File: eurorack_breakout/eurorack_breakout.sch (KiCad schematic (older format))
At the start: 11 parts, among them J1 Conn_02x08_Odd_Even, J2 Conn_01x08_Male, U1 LM1117-3.3, U2 LM1117-5.0

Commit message: eh, different license
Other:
- note added: "(c) 2021 Zachary Hart\nCC BY-SA-4.0\nrev0.1"
- note removed: "(c) 2021 Zachary Hart\nCC BY-NC-SA\n"
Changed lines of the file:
@@
 Text Notes 8400 7750 2    69   Italic 14
 16-Pin Eurorack Power Breakout
-Text Notes 6300 6950 0    49   ~ 0
-(c) 2021 Zachary Hart\nCC BY-NC-SA\n
+Text Notes 6300 7050 0    49   ~ 0
+(c) 2021 Zachary Hart\nCC BY-SA-4.0\nrev0.1
 $EndSCHEMATC

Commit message: board rev0.2
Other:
- note added: "(c) 2021 Zachary Hart\nCC BY-SA-4.0\nschematic rev0.1"
- note removed: "(c) 2021 Zachary Hart\nCC BY-SA-4.0\nrev0.1"
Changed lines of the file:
@@
 16-Pin Eurorack Power Breakout
 Text Notes 6300 7050 0    49   ~ 0
-(c) 2021 Zachary Hart\nCC BY-SA-4.0\nrev0.1
+(c) 2021 Zachary Hart\nCC BY-SA-4.0\nschematic rev0.1
 $EndSCHEMATC

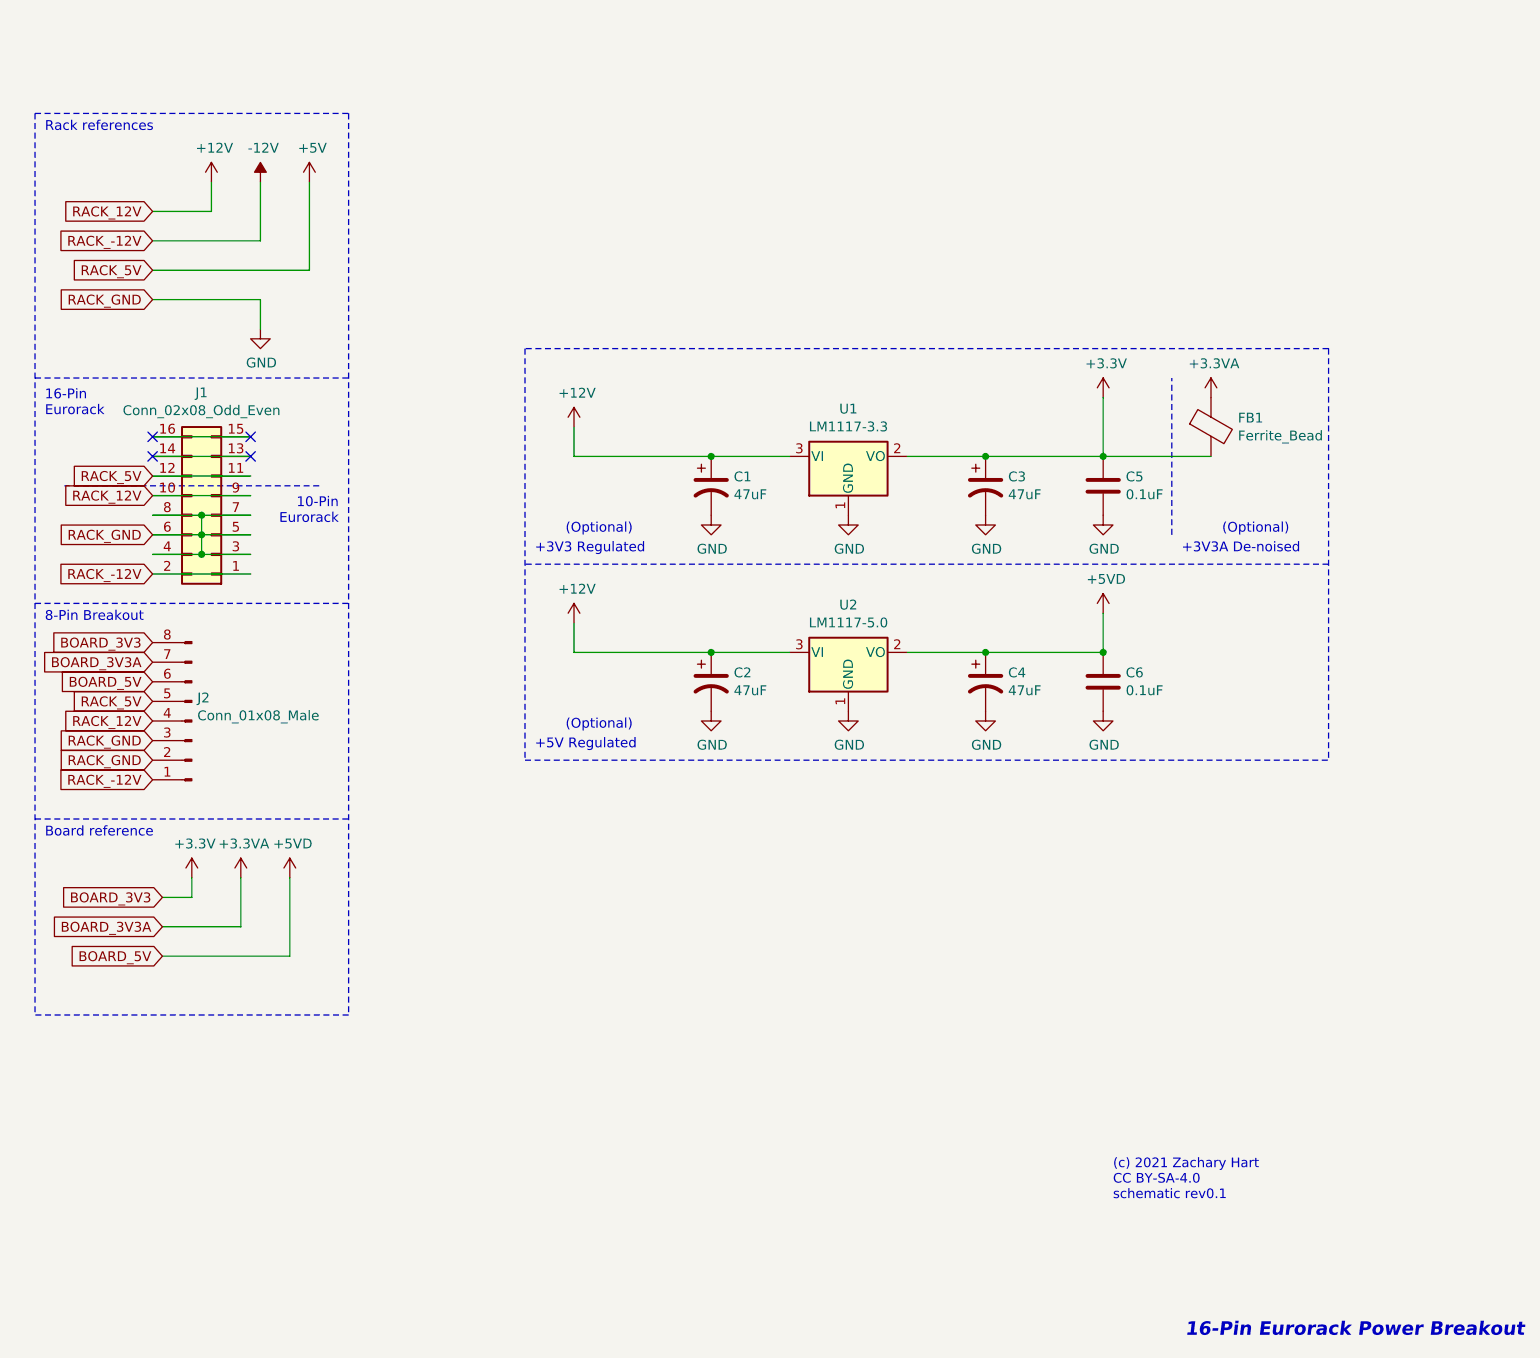
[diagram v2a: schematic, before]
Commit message: Board rev0.3, new license, cleanup
- Removed unneeded KiCad files
- Updated license to CERN-OHL-P v2
- Updated README
- Project-level footprint library
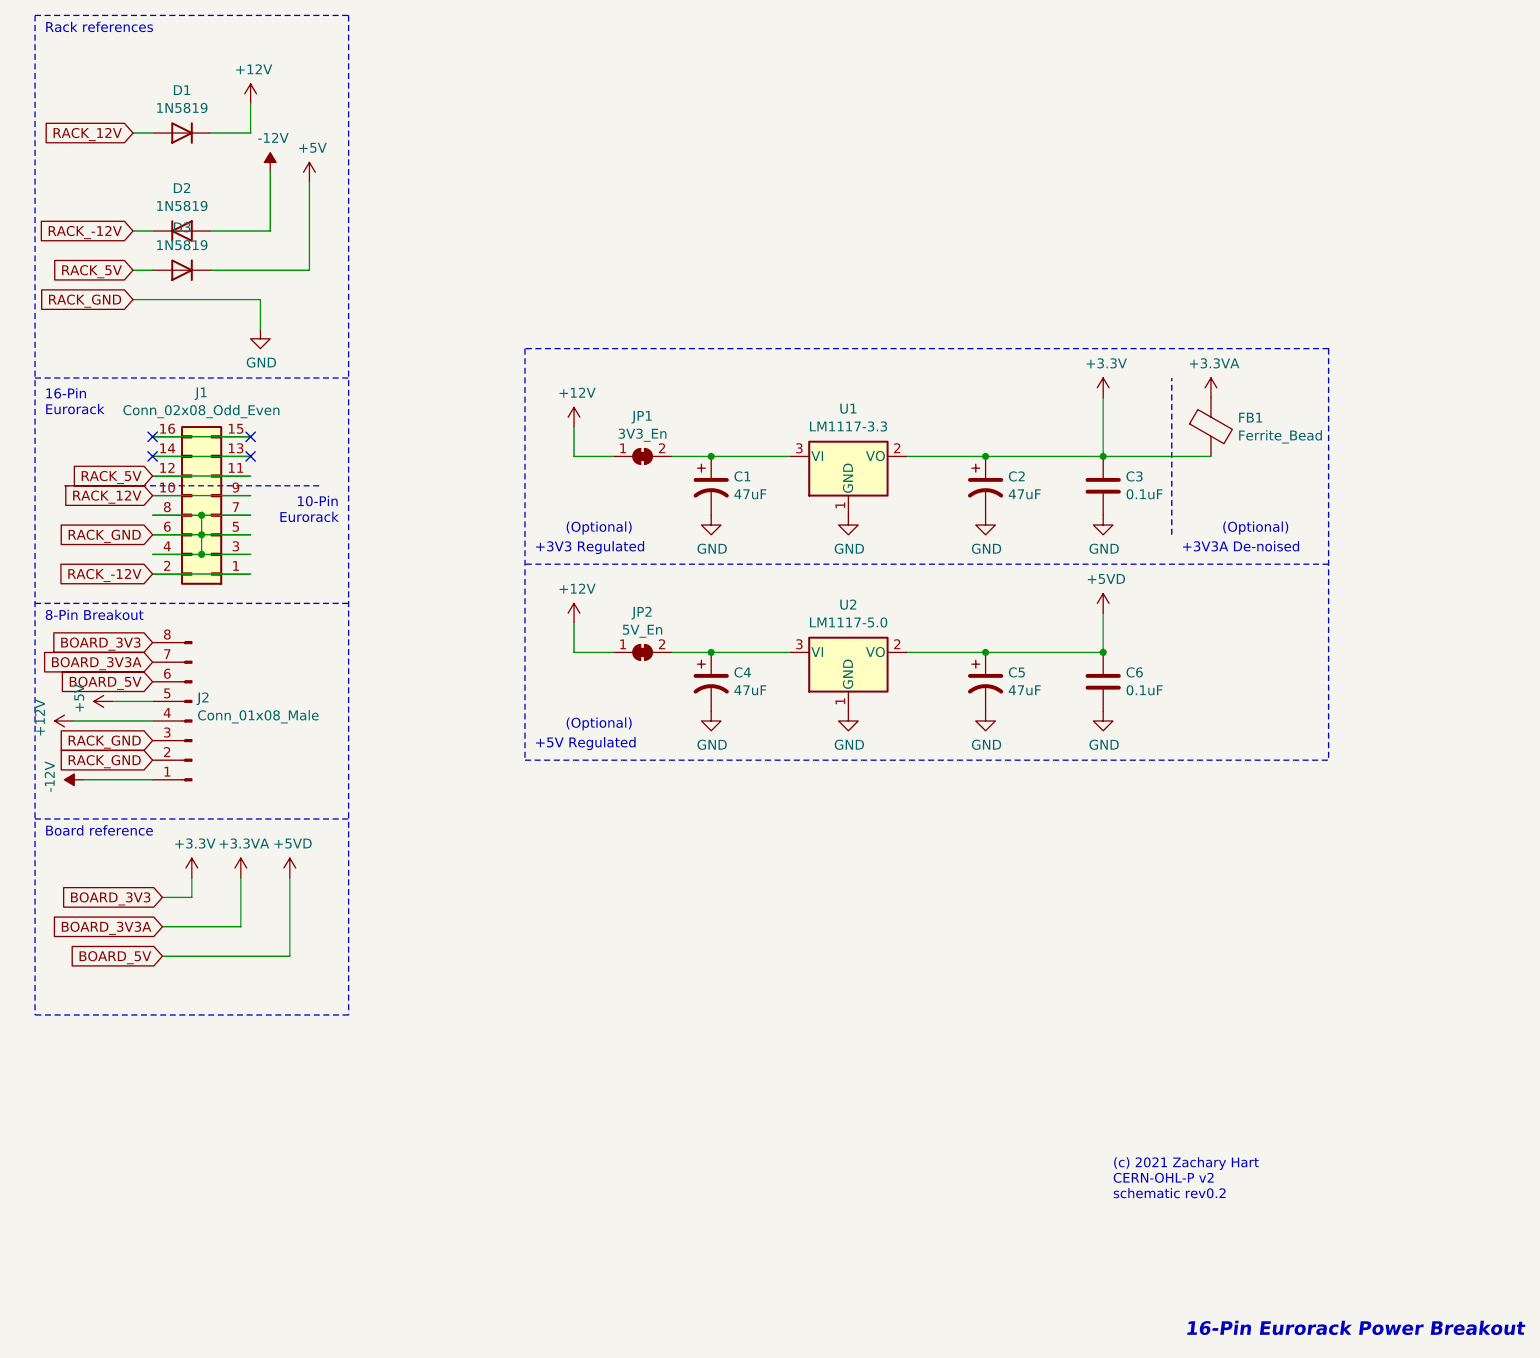
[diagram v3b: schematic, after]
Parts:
- added D1, D2, D3: 1N5819, Diode_SMD:D_SOD-123, symbol Device:D
- added JP1: 3V3_En, Jumper:SolderJumper-2_P1.3mm_Bridged_RoundedPad1.0x1.5mm, symbol Jumper:SolderJumper_2_Bridged
- added JP2: 5V_En, Jumper:SolderJumper-2_P1.3mm_Bridged_RoundedPad1.0x1.5mm, symbol Jumper:SolderJumper_2_Bridged
- renumbered C3 to C2, C5 to C3, C2 to C4, C4 to C5
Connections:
- net +12V: now also D1.1 (K), JP1.1 (A), JP2.1 (A); no longer C1.1, C4.1, J1.10 (Pin_10), J1.9 (Pin_9), U1.3 (VI), U2.3 (VI)
- net +5V: now also D3.1 (K); no longer J1.11 (Pin_11), J1.12 (Pin_12)
- net -12V: now also D2.2 (A); no longer J1.1 (Pin_1), J1.2 (Pin_2)
- new net: C4.1, JP2.2 (B), U2.3 (VI)
- new net: C1.1, JP1.2 (B), U1.3 (VI)
- new net RACK_-12V: D2.1 (K), J1.1 (Pin_1), J1.2 (Pin_2)
- new net RACK_12V: D1.2 (A), J1.10 (Pin_10), J1.9 (Pin_9)
- new net RACK_5V: D3.2 (A), J1.11 (Pin_11), J1.12 (Pin_12)
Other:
- note added: "(c) 2021 Zachary Hart\nCERN-OHL-P v2\nschematic rev0.2"
- note removed: "(c) 2021 Zachary Hart\nCC BY-SA-4.0\nschematic rev0.1"
